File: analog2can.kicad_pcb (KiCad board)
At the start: 4 copper layers, 100 x 50 mm, 91 parts, among them J1 Conn_01x04, J2 DA15_Socket, J3 DT13-4P, J4 Conn_ARM_SWD_TagConnect_TC203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, U1 TJA1051T-E, U2 STM32U535CBTx, U3 TPS26400PWP, U4 TPS62932, U5 TLV75733PDBV, Y1 ABM8-16.000MHZ-D1X-T

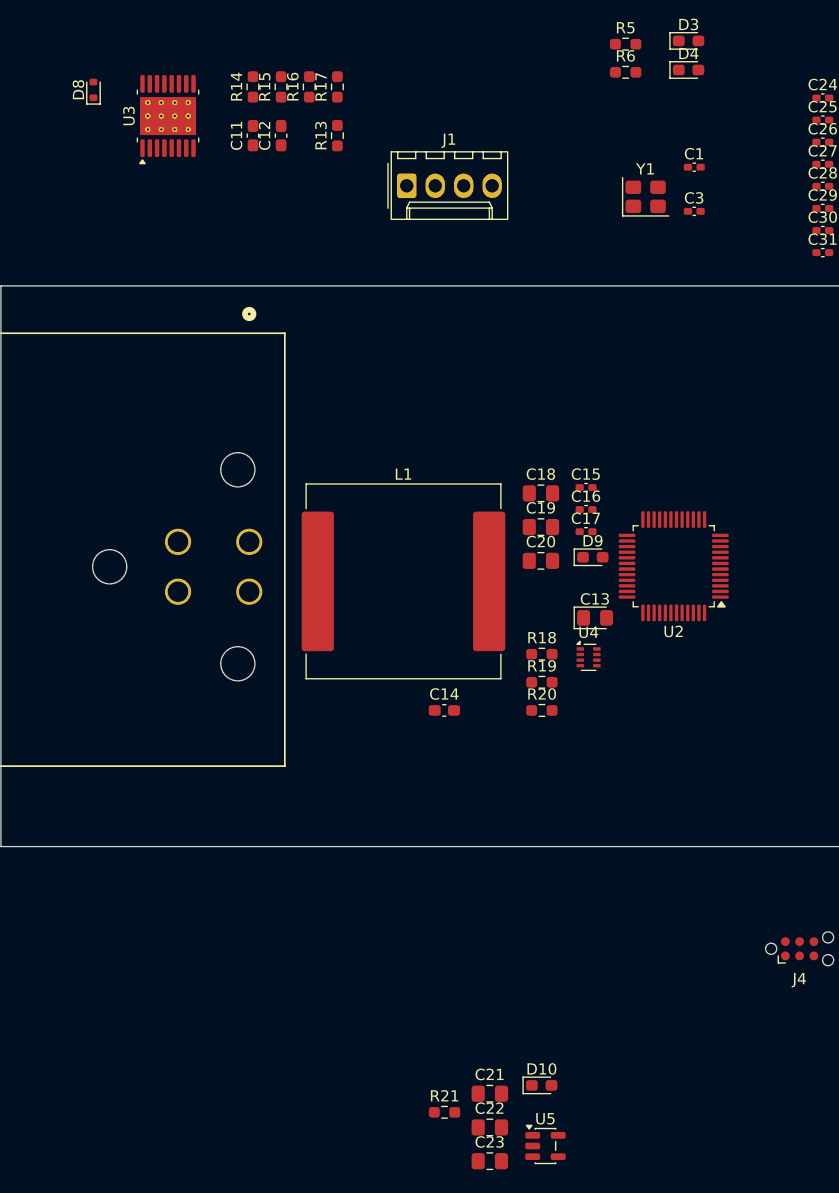
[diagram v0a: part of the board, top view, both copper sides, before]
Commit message: Fin layout buck, debut layout efuse
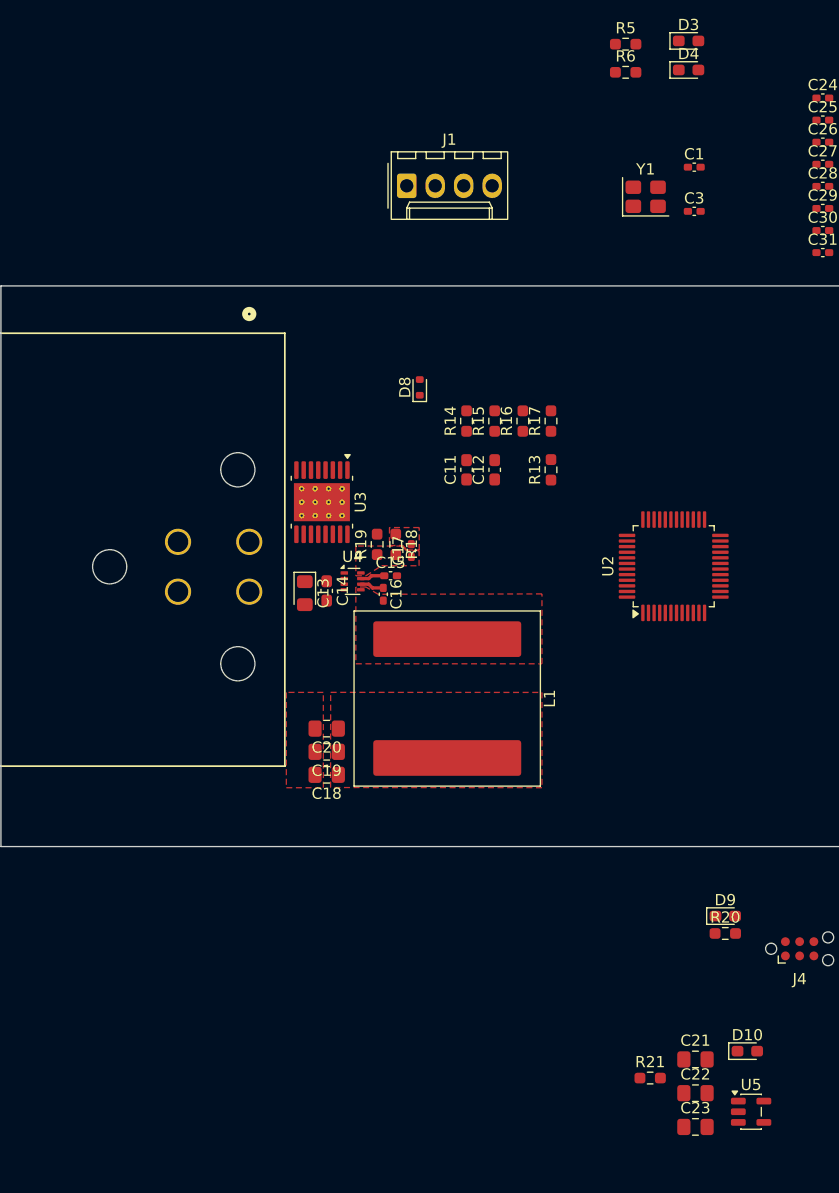
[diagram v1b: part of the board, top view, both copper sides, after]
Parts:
- L1: footprint Inductor_SMD:L_Vishay_IHLP-6767 -> Inductor_SMD:L_Coilcraft_XAL1510-333
- moved D8 39.4 mm to (157.1, 77.5)
- moved U3 37.1 mm to (148.3, 87.7), turned to -90 degrees
- moved C12 35.4 mm to (163.7, 84.8)
- moved R15 35.4 mm to (163.7, 80.5)
- moved R16 35.4 mm to (166.2, 80.5)
- moved C11 35.4 mm to (161.2, 84.8)
- moved R13 35.4 mm to (168.8, 84.8)
- moved R14 35.4 mm to (161.2, 80.5)
- moved R17 35.4 mm to (168.8, 80.5)
- moved D9 34.1 mm to (184.3, 124.7)
- moved C18 31.5 mm to (148.8, 112.0), turned to 180 degrees
- moved C19 27.7 mm to (148.8, 110.0), turned to 180 degrees
- moved C13 26.0 mm to (146.8, 95.8), turned to -90 degrees
- moved R20 25.8 mm to (184.3, 126.2)
- moved C20 24.3 mm to (148.8, 107.9), turned to 180 degrees
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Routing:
- net Net-(U4-SS): track 0.00 -> 2.19 mm
- net Net-(U4-BST): track 0.00 -> 2.14 mm
- added copper zone on F.Cu, net +5V
- added copper zone on In2.Cu, net +5V
- added copper zone on F.Cu, net GND
- added copper zone on In1.Cu, net GND
- added copper zone on F.Cu, net Net-(U4-FB)

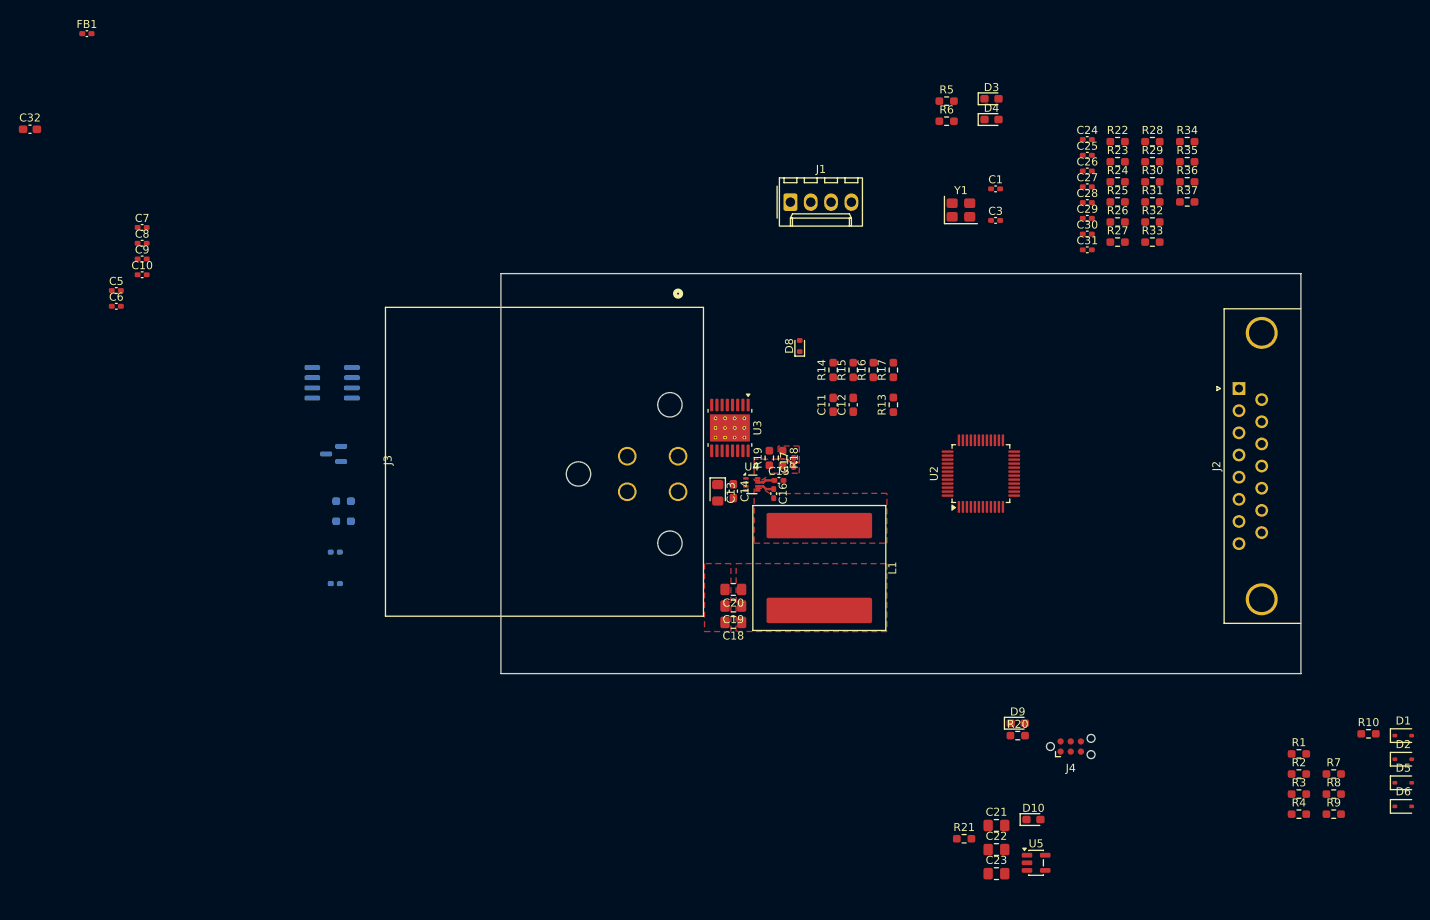
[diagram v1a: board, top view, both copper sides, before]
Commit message: fin layout power supply (sauf LDO), debut layout MCU
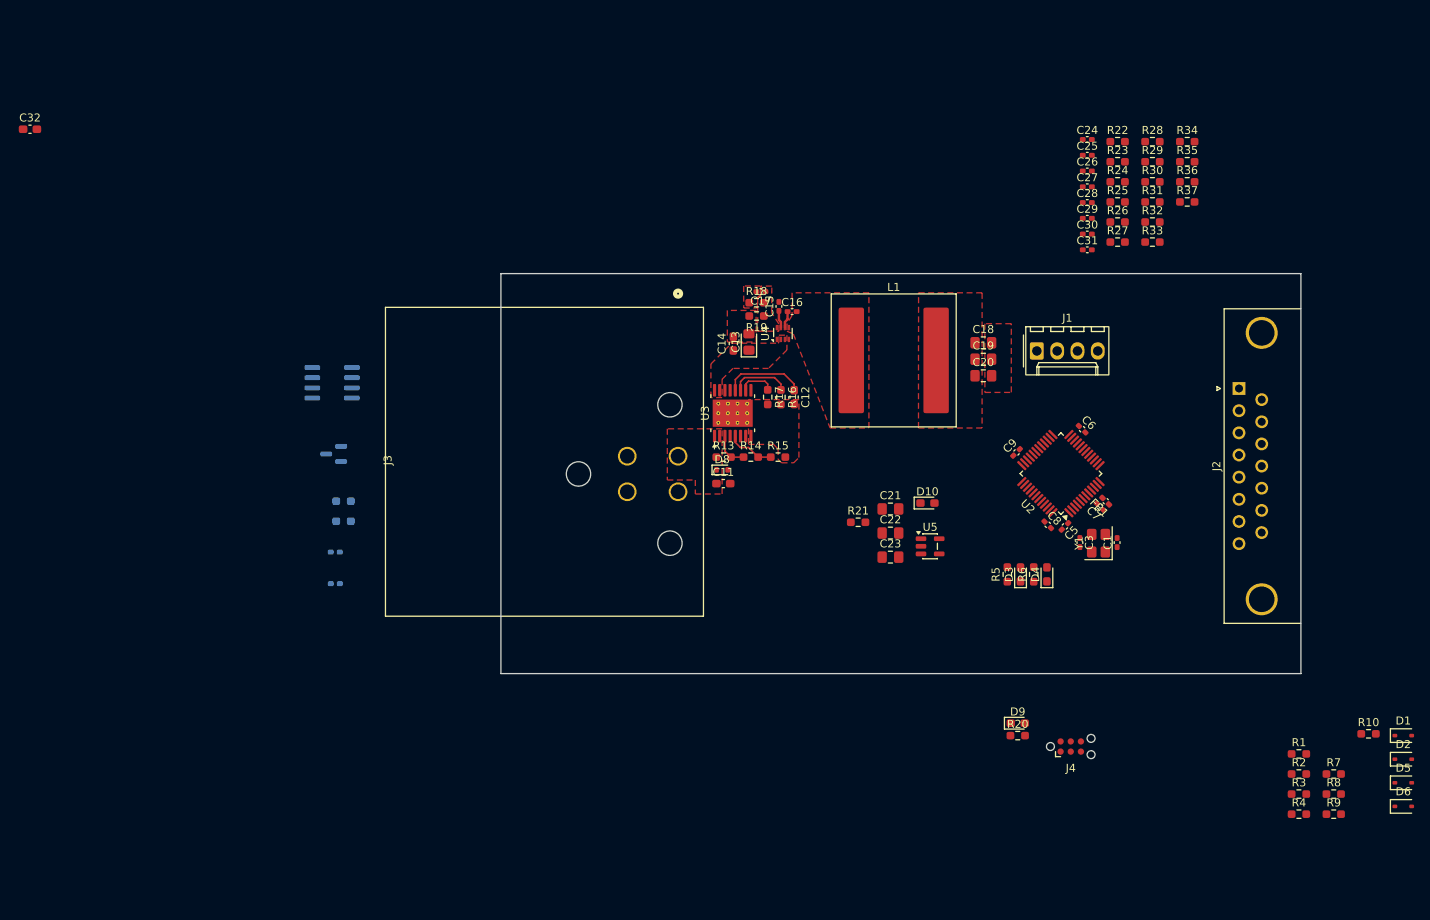
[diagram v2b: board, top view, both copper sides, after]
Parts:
- removed C10: 0.1u, Capacitor_SMD:C_0402_1005Metric_Pad0.74x0.62mm_HandSolder
- moved FB1 140.1 mm to (195.3, 96.9), turned to 135 degrees
- moved C7 124.7 mm to (194.6, 97.6), turned to 135 degrees
- moved C5 122.2 mm to (190.2, 100.0), turned to -135 degrees
- moved C6 121.7 mm to (192.3, 87.9), turned to -45 degrees
- moved C8 118.5 mm to (188.1, 99.8), turned to -45 degrees
- moved C9 111.9 mm to (184.2, 90.8), turned to 45 degrees
- moved R5 59.6 mm to (183.0, 106.0), turned to 90 degrees
- moved D3 59.6 mm to (184.7, 106.0), turned to 90 degrees
- moved R6 57.7 mm to (186.3, 106.0), turned to 90 degrees
- moved D4 57.3 mm to (187.9, 106.0), turned to 90 degrees
- moved C18 46.9 mm to (180.0, 77.1), turned to 0 degrees
- moved C1 46.7 mm to (196.7, 102.1), turned to 90 degrees
- moved Y1 45.1 mm to (194.4, 102.2), turned to 90 degrees
- moved C19 43.9 mm to (180.0, 79.2), turned to 0 degrees
- moved C23 41.7 mm to (168.4, 103.9)
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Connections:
- C2 pad 1: +3.3V -> +5V
- U1 pad 3: +3.3V -> +5V
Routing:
- net Net-(U3-dVdT): track 0.00 -> 10.3 mm
- net Net-(U3-ILIM): track 0.00 -> 7.41 mm
- net Net-(U3-OVP): track 0.00 -> 5.97 mm
- net Net-(U3-IMON): track 0.00 -> 4.56 mm
- net Net-(U3-UVLO): track 0.00 -> 4.51 mm
- added copper zone on F.Cu, net +12V
- added copper zone on F.Cu, net /power (done)/RTN
